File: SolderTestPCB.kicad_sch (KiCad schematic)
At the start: 11 parts, among them J1 CON_INPUT, J2 CON_I2C, J3 CON_SERIAL, SW1 SW_RST, SW2 SW_PRG, U1 ESP-12

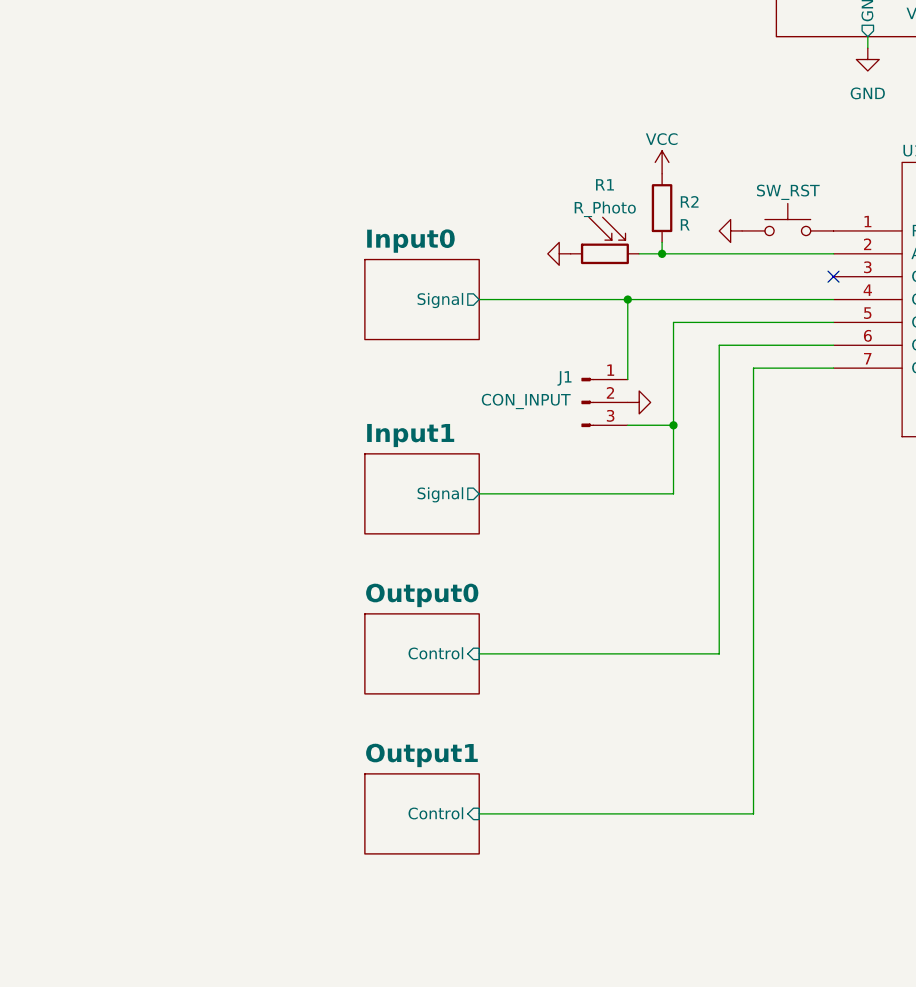
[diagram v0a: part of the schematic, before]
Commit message: Schematic ready; PCB needs silkscreen
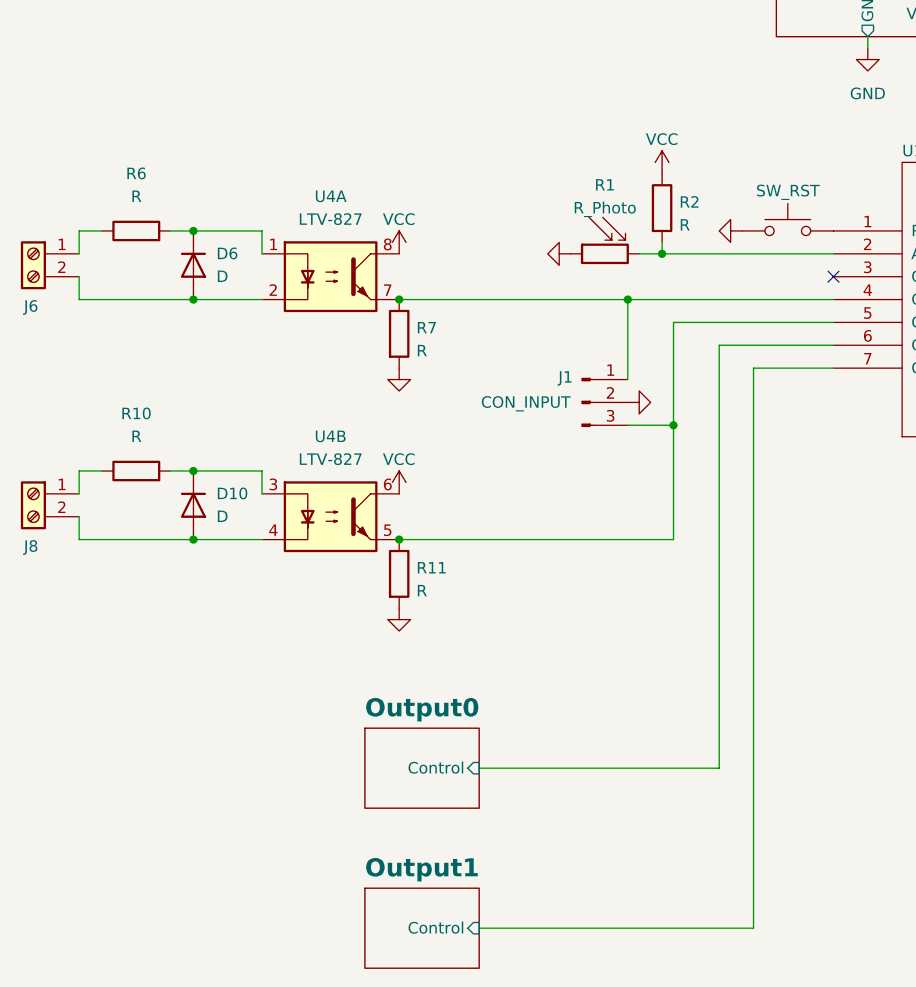
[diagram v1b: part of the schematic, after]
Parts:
- added D10, D6: D, Diode_THT:D_DO-41_SOD81_P2.54mm_Vertical_AnodeUp, symbol Device:D
- added J6, J8: Screw_Terminal_01x02, TerminalBlock_RND:TerminalBlock_RND_205-00001_1x02_P5.00mm_Horizontal, symbol Connector:Screw_Terminal_01x02
- added R10, R11, R6, R7: R, Resistor_THT:R_Axial_DIN0204_L3.6mm_D1.6mm_P1.90mm_Vertical, symbol Device:R
- added U4: LTV-827, Package_DIP:DIP-8_W7.62mm, symbol Isolator:LTV-827
- C1: footprint (none) -> Capacitor_THT:C_Disc_D3.8mm_W2.6mm_P2.50mm
- J1, J2, J3: footprint (none) -> Connector_PinHeader_2.54mm:PinHeader_1x03_P2.54mm_Vertical
- R1: footprint (none) -> OptoDevice:R_LDR_5.1x4.3mm_P3.4mm_Vertical
- R2, R3, R4: footprint (none) -> Resistor_THT:R_Axial_DIN0204_L3.6mm_D1.6mm_P1.90mm_Vertical
- SW1, SW2: footprint (none) -> Button_Switch_THT:SW_PUSH_6mm_H4.3mm
- U1: footprint (none) -> RF_Module:HOPERF_RFM9XW_THT
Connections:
- net GND: now also R11.2, R7.2
- net VCC: now also U4.6, U4.8
- net Input0/Signal: no longer names the net of J1.1 (Pin_1), U1.4 (GPIO16)
- net Input0/Signal: now also R7.1, U4.7
- net Input1/Signal: no longer names the net of J1.3 (Pin_3), U1.5 (GPIO14)
- net Input1/Signal: now also R11.1, U4.5
- new net: D10.1 (K), R10.2, U4.3
- new net: D10.2 (A), J8.2 (Pin_2), U4.4
- new net: J8.1 (Pin_1), R10.1
- new net: D6.1 (K), R6.2, U4.1
- new net: D6.2 (A), J6.2 (Pin_2), U4.2
- new net: J6.1 (Pin_1), R6.1
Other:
- removed sheet Input0
- removed sheet Input1

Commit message: PCB Layout finished (RTM)
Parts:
- added H1, H2, H3, H4: MountingHole, MountingHole:MountingHole_3.2mm_M3, symbol Mechanical:MountingHole
- D10, D6: footprint Diode_THT:D_DO-41_SOD81_P2.54mm_Vertical_AnodeUp -> Diode_THT:D_DO-15_P10.16mm_Horizontal
